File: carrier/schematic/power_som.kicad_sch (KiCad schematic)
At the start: 11 parts, among them J29002 TYPE-C-31-M-12, U29001 TPS2051CDBVR, U29002 USBLC6-2SC6

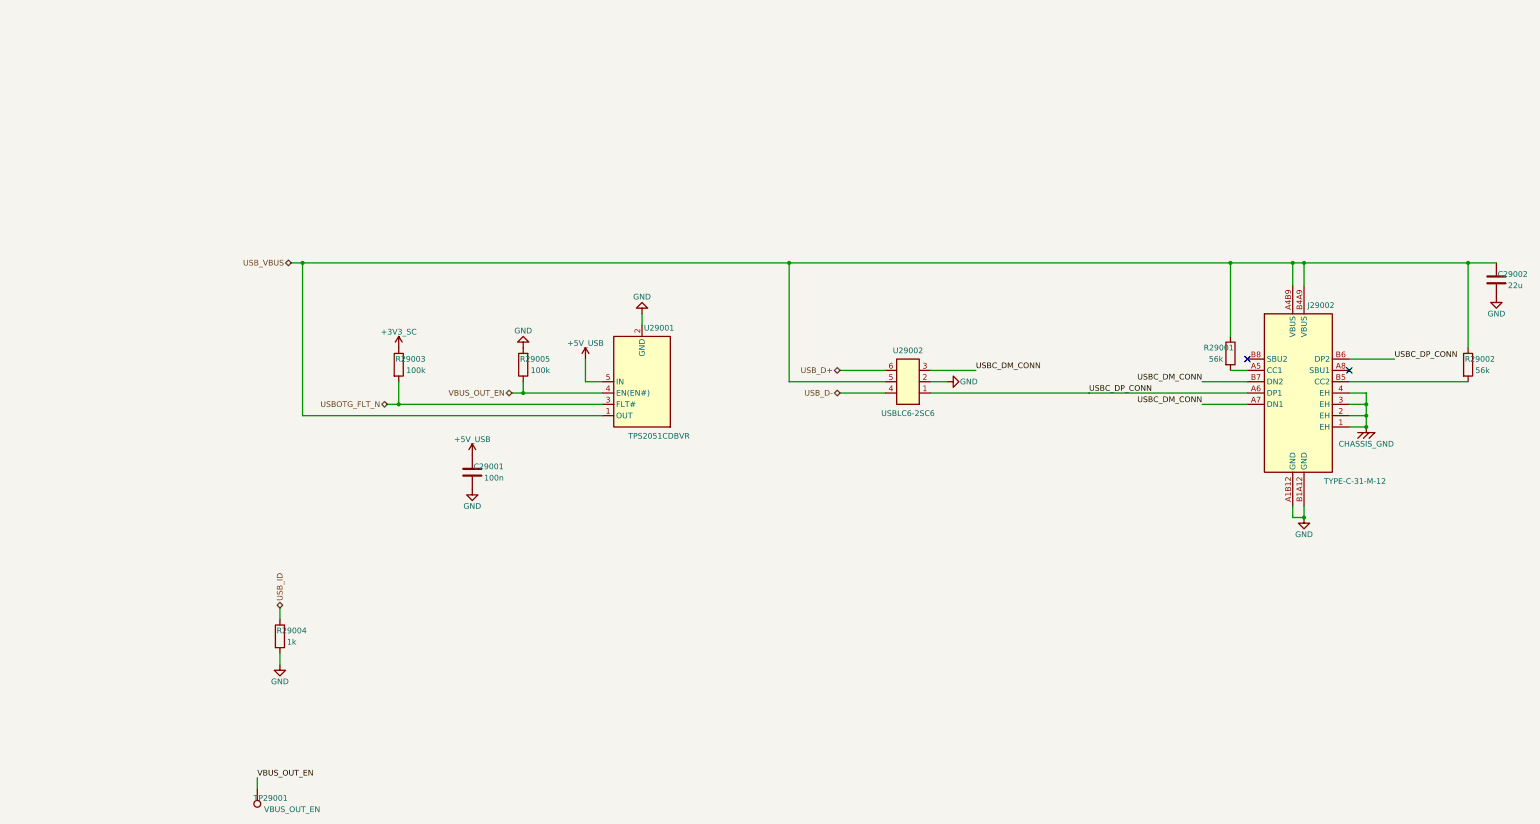
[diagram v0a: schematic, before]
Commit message: buck U1 -> LMR33630 EP buck: power_som split + placer regulator-template generalization
LANDS the exposed-pad buck reselect (the whole point: U1 was a bare TSOT-23-6
TPS54302 with no thermal pad). U1 is now the LMR33630ADDAR (LCSC C841384): TI
SIMPLE SWITCHER, synchronous + internally compensated, 3.8-36 V / 3 A, HSOIC-8
PowerPAD with a REAL datasheet exposed pad, EP (pad 9) netted to GND. Uses the
KiCad STOCK symbol Regulator_Switching:LMR33640ADDA (same DDA pinout, proper
power_in VIN) + the faithful EP-bearing footprint — exactly the TPS54302/
AP2112K stock-symbol idiom. VFB 1.0 V -> 40.2k/10k FB divider = 5.02 V.

SHEET SPLIT (power -> power + power_som): the larger LMR33630 pushed the
4-converter power sheet past one A3 page. The +5V_SOM always-on stage (U4) is
the cleanly-separable unit (only +VIN/+5V_SOM/GND rails cross — they merge by
name; every signal net is internal) and moves to its own subsystem power_som.py.
An auto-paginator cannot split this sheet from the netlist alone (its regulators
chain-share input/output rails, so shared decoupling caps can't be assigned to a
stage); the human split assigns them explicitly. board LINK proves +5V_SOM
merges power_som<->som_j1 and +VIN across pd_input/power/power_mon/power_som.

PLACER GENERALIZATION (schgen/place.py, regulator template) so a richer buck
than the TPS54302's exact 6-pin pinout places — all verified byte-identical for
the 28 unchanged sheets (per-sheet), board gate PASS:
  - _detect_stages: a switch/output pin may be 'output' (LMR SW) not just
    'power_out' (TPS54302 SW); LDO branch stays strict to power_out.
  - _stage_row Edit 1+3: place an aux internal-LDO bias output (LMR VCC, pin 6)
    + its single bypass cap in its own left column (was the "U1_VCC islet, opens
    forbidden" open); emit ALL distinct bottom GND/EP points (not just the last);
    emit explicit NC markers for authored no-connects (the LMR open-collector PG
    pin 4 — was an ERC "Pin not connected").
  - _stage_row Edit 2: ro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
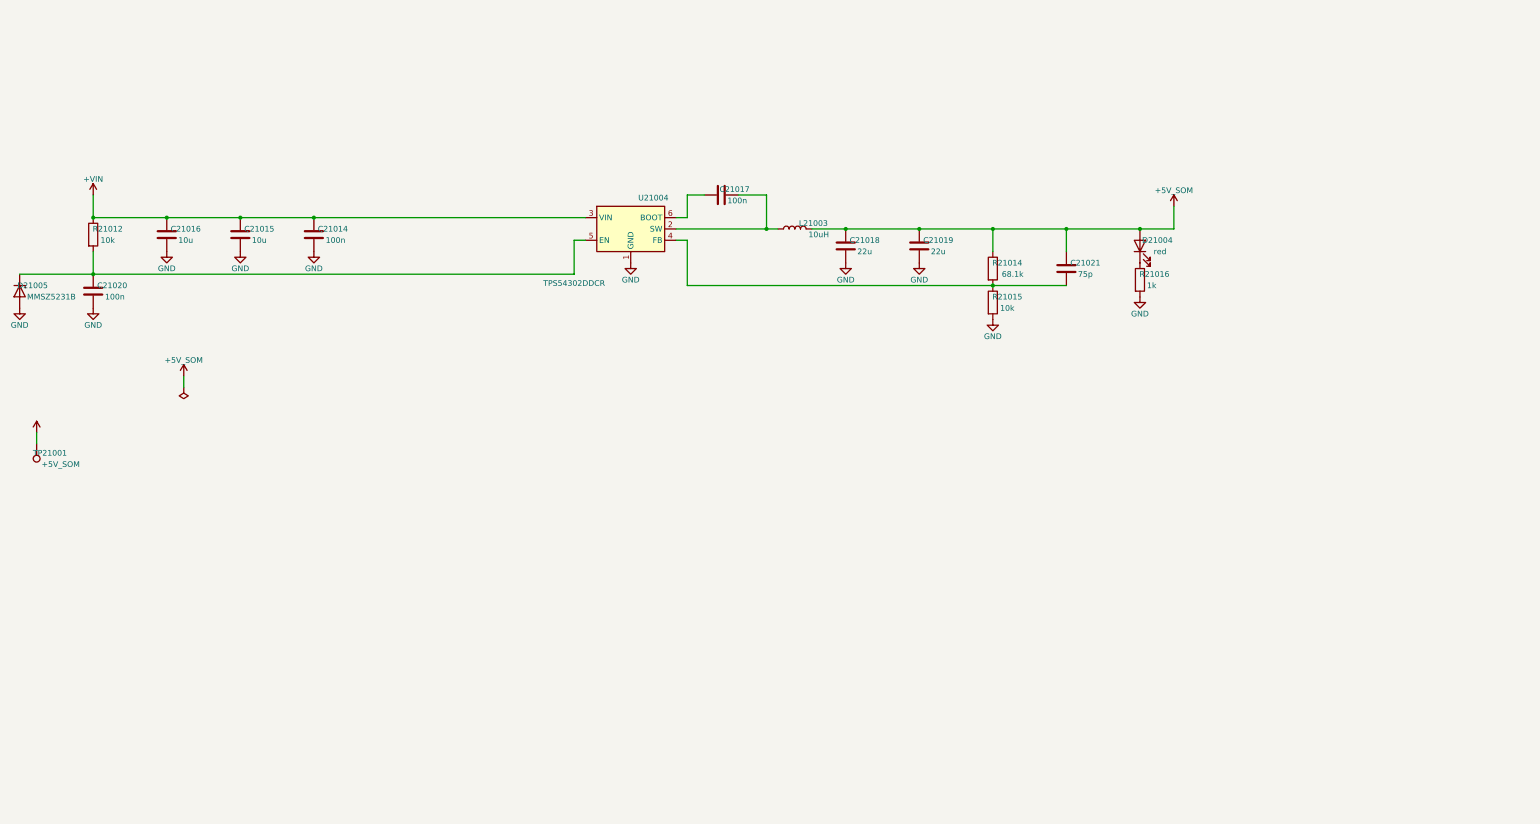
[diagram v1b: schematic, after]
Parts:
- removed C29001: 100n, Capacitor_SMD:C_0603_1608Metric, symbol Device:C
- removed C29002: 22u, Capacitor_SMD:C_0805_2012Metric, symbol Device:C
- removed J29002: TYPE-C-31-M-12, TYPE-C-31-M-12:TYPE-C-31-M-12, symbol TYPE-C-31-M-12:TYPE-C-31-M-12
- removed R29001, R29002: 56k, Resistor_SMD:R_0603_1608Metric, symbol Device:R
- removed R29003, R29005: 100k, Resistor_SMD:R_0603_1608Metric, symbol Device:R
- removed R29004: 1k, Resistor_SMD:R_0603_1608Metric, symbol Device:R
- removed TP29001: VBUS_OUT_EN, TestPoint:TestPoint_Pad_D1.5mm, symbol Connector:TestPoint
- removed U29001: TPS2051CDBVR, TPS2051CDBVR:TPS2051CDBVR, symbol TPS2051CDBVR:TPS2051CDBVR
- removed U29002: USBLC6-2SC6, USBLC6-2SC6:USBLC6-2SC6, symbol USBLC6-2SC6:USBLC6-2SC6
- added C21014, C21017, C21020: 100n, Capacitor_SMD:C_0603_1608Metric, symbol Device:C
- added C21015, C21016: 10u, Capacitor_SMD:C_1206_3216Metric, symbol Device:C
- added C21018, C21019: 22u, Capacitor_SMD:C_0805_2012Metric, symbol Device:C
- added C21021: 75p, Capacitor_SMD:C_0603_1608Metric, symbol Device:C
- added D21004: red, LED_SMD:LED_0603_1608Metric, symbol Device:LED
- added D21005: MMSZ5231B, Diode_SMD:D_SOD-123, symbol Device:D_Zener
- added L21003: 10uH, SWPA8040S100MT:SWPA8040S100MT, symbol Device:L
- added R21012, R21015: 10k, Resistor_SMD:R_0603_1608Metric, symbol Device:R
- added R21014: 68.1k, Resistor_SMD:R_0603_1608Metric, symbol Device:R
- added R21016: 1k, Resistor_SMD:R_0603_1608Metric, symbol Device:R
- added TP21001: +5V_SOM, TestPoint:TestPoint_Pad_D1.5mm, symbol Connector:TestPoint
- added U21004: TPS54302DDCR, Package_TO_SOT_SMD:TSOT-23-6, symbol Regulator_Switching:TPS54302
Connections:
- net GND: now also C21014.2, C21015.2, C21016.2, C21018.2, C21019.2, C21020.2, D21005.2 (A), R21015.2, R21016.2, U21004.1 (GND)
- new net: C21021.2, R21014.2, R21015.1, U21004.4 (FB)
- new net: C21020.1, D21005.1 (K), R21012.2, U21004.5 (EN)
- new net: C21017.2, L21003.1, U21004.2 (SW)
- new net: C21017.1, U21004.6 (BOOT)
- new net: D21004.1 (K), R21016.1
- new net +5V_SOM: C21018.1, C21019.1, C21021.1, D21004.2 (A), L21003.2, R21014.1, TP21001.1
- new net +VIN: C21014.1, C21015.1, C21016.1, R21012.1, U21004.3 (VIN)
- no-connect marks 2 -> 0
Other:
- title: USB 2.0 HS OTG port (Type-C, host) -> Power: +VIN -> +5V_SOM always-on buck (SoM VIN, P0 fix)

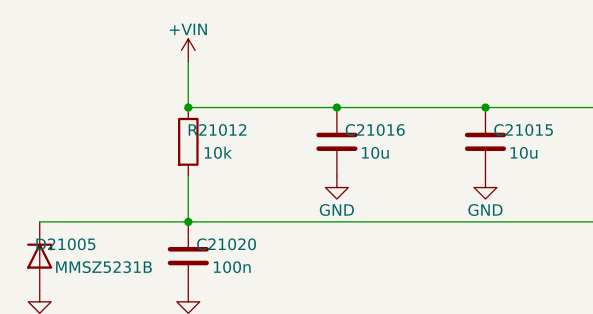
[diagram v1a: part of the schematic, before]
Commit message: carrier: regen artifacts — DEF-D shunt split (power/power_mon/power_som + downstream)
Co-Authored-By: Claude Opus 4.8 <noreply@anthropic.com>
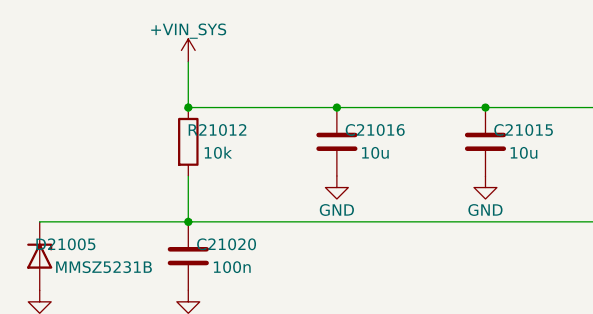
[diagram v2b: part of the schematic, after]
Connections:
- net +VIN renamed +VIN_SYS
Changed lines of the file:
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@@
 	)
 	(symbol
-		(lib_id "schgen:+VIN")
+		(lib_id "schgen:+VIN_SYS")
 		(at 34.29 72.39 0)
 		(unit 1)
@@
 		(property
 			"Value"
-			"+VIN"
+			"+VIN_SYS"
 			(at 34.29 68.834 0)
 			(effects
